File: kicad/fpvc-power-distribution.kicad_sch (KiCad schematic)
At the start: 43 parts, among them J1 Solenoid1, J2 PLC-S1, J3 Solenoid1, J4 PLC-S2, J5 Clutch, J6 PLC-C, J7 Vin_24V, J8 V_PLC, J9 V_Screen, Q1 IRLZ44N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

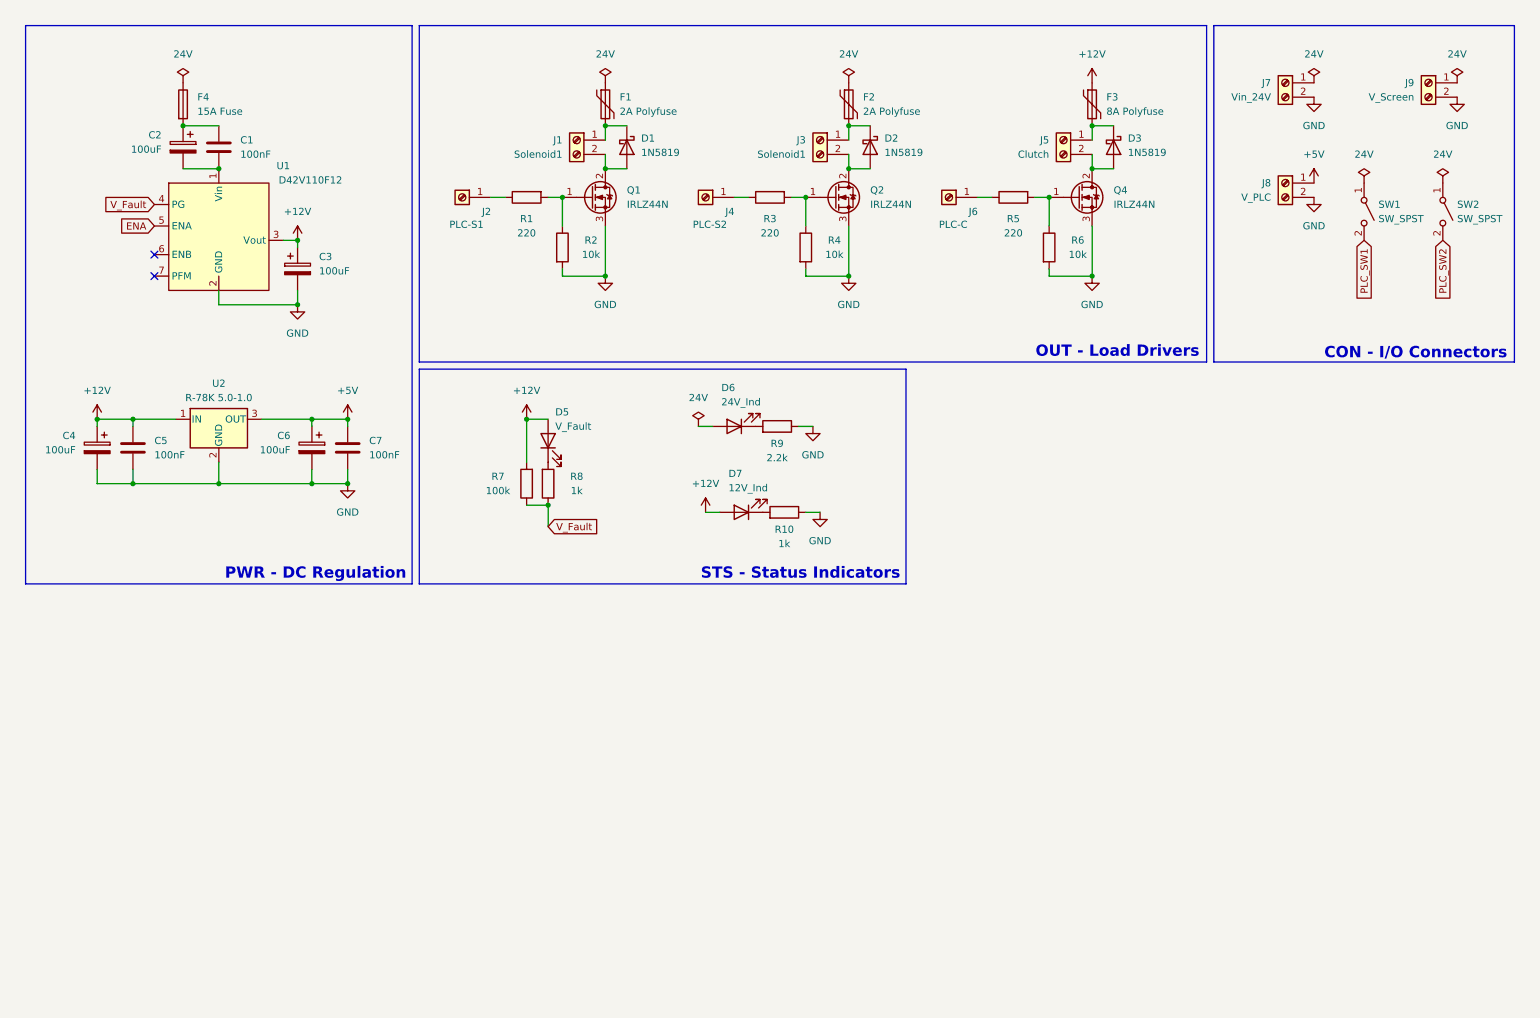
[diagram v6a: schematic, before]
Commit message: feat: Update schematic with GPIO connectors
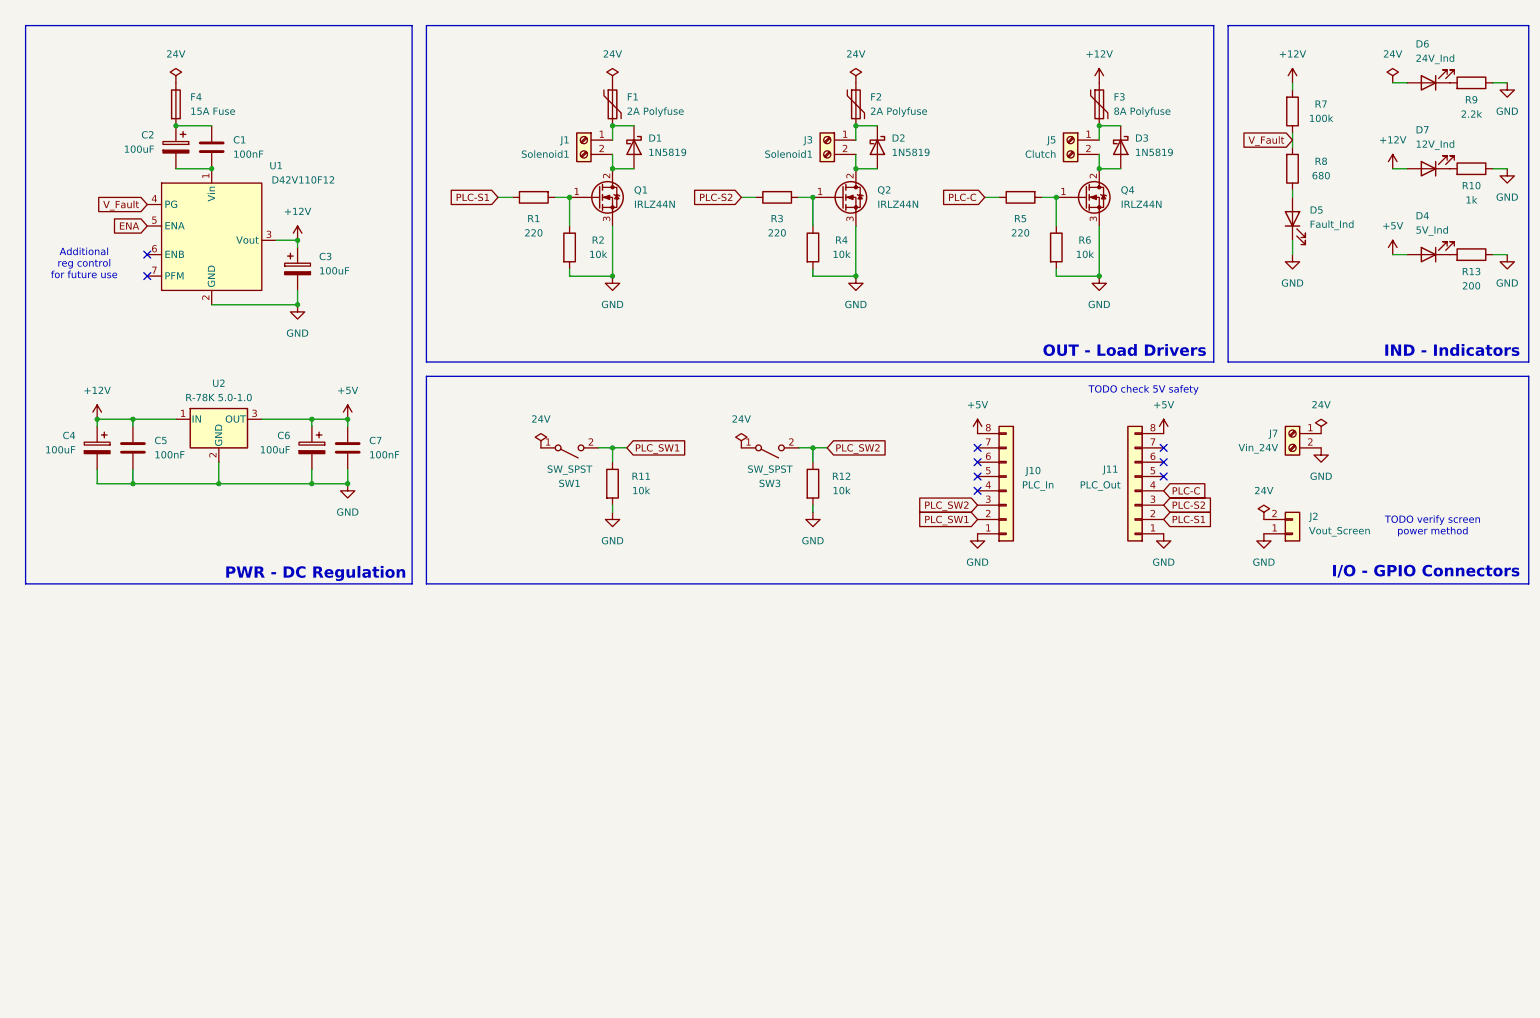
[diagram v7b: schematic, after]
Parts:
- removed J2: PLC-S1, symbol Connector:Screw_Terminal_01x01
- removed J4: PLC-S2, symbol Connector:Screw_Terminal_01x01
- removed J6: PLC-C, symbol Connector:Screw_Terminal_01x01
- removed J8: V_PLC, symbol Connector:Screw_Terminal_01x02
- removed J9: V_Screen, symbol Connector:Screw_Terminal_01x02
- removed SW2: SW_SPST, symbol Switch:SW_SPST
- added D4: 5V_Ind, symbol Device:LED
- added J10: PLC_In, symbol Connector_Generic:Conn_01x08
- added J11: PLC_Out, symbol Connector_Generic:Conn_01x08
- added J2: Vout_Screen, symbol Connector_Generic:Conn_01x02
- added R11, R12: 10k, symbol Device:R
- added R13: 200, symbol Device:R
- added SW3: SW_SPST, symbol Switch:SW_SPST
- D5: value V_Fault -> Fault_Ind
- R8: value 1k -> 680
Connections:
- net +12V: no longer D5.2 (A)
- net +5V: now also D4.2 (A), J10.8 (Pin_8), J11.8 (Pin_8)
- net GND: now also D5.1 (K), J10.1 (Pin_1), J11.1 (Pin_1), J2.1 (Pin_1), R11.2, R12.2, R13.1
- net PLC_SW1: now also J10.2 (Pin_2), R11.1
- net PLC_SW2: now also J10.3 (Pin_3), R12.1, SW3.2 (B)
- net V_Fault: now also R8.2; no longer R8.1
- net PLC-S1: now reaches R1.1
- net PLC-S1: now also J11.2 (Pin_2)
- net PLC-C: now reaches R5.1
- net PLC-C: now also J11.4 (Pin_4)
- net PLC-S2: now reaches R3.1
- net PLC-S2: now also J11.3 (Pin_3)
- new net: D4.1 (K), R13.2
- new net: D5.2 (A), R8.1
- no-connect marks 2 -> 9
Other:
- note added: "Additional reg control for future use"
- note added: "I/O - GPIO Connectors"
- note added: "IND - Indicators"
- note added: "TODO check 5V safety"
- note added: "TODO verify screen power method"
- note removed: "CON - I/O Connectors"
- note removed: "STS - Status Indicators"
- moved on the sheet: C1, C2, D1, D2, D3, D5, D6, D7, F1, F2, F3, F4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

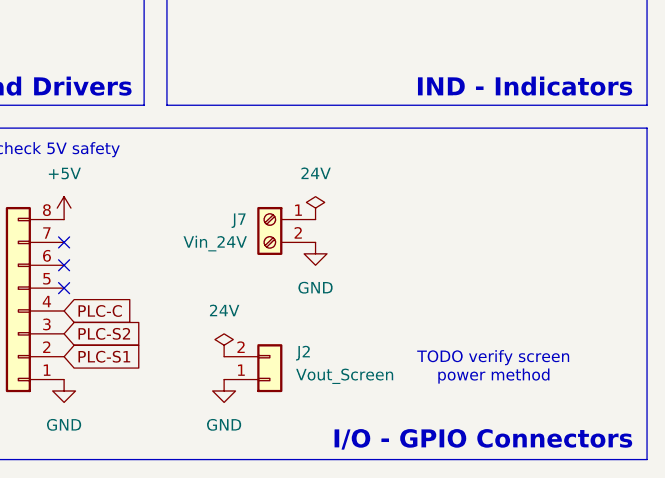
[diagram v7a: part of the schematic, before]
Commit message: fix: Add decoupling caps to screen power connector
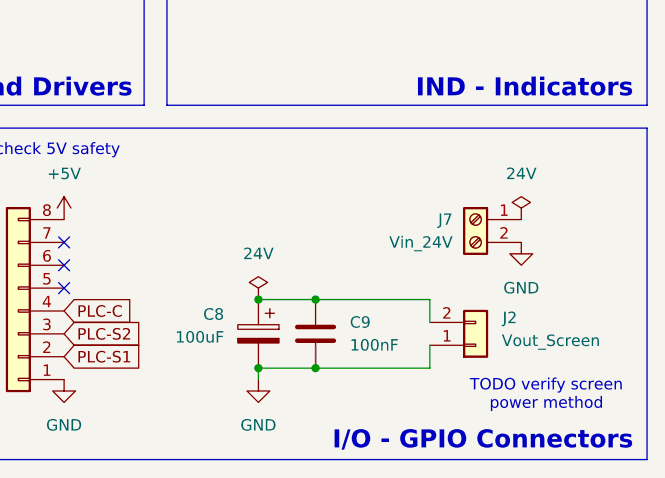
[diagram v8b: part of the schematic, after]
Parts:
- added C8: 100uF, symbol Device:C_Polarized
- added C9: 100nF, symbol Device:C
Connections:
- net GND: now also C8.2, C9.2
- net at J2.2 (Pin_2): now also C8.1, C9.1
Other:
- moved on the sheet: J2, J7
